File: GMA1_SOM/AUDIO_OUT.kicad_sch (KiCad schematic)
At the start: 1 part, among them U5 MAX98357B

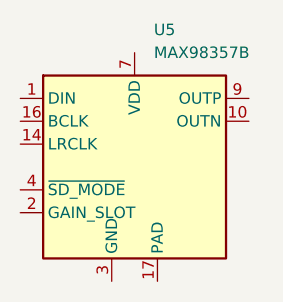
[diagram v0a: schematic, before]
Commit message: add display and ram
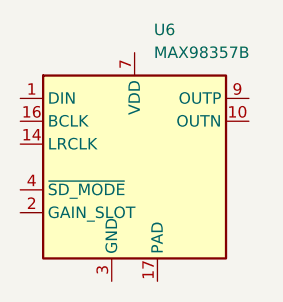
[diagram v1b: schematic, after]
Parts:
- renumbered U5 to U6
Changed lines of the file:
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@@
 		(dnp no)
 		(fields_autoplaced yes)
-		(property "Reference" "U5"
+		(property "Reference" "U6"
 			(at 162.1633 74.93 0)
 			(effects
@@
 			(project ""
 				(path "/d784c6f3-1f62-4397-857c-3a97e2a0cbd1/9d08b115-8d2a-4cae-b926-cec128a135e3/28126a2f-6470-4e65-a324-bd80a9b9c626"
-					(reference "U5")
+					(reference "U6")
 					(unit 1)
 				)
